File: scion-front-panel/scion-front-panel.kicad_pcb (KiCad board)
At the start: 4 copper layers, 275 x 39.5 mm, 62 parts, among them J1 SEND_VS, J10 SEND_Y3, J11 SEND_U3, J12 SEND_V3, J13 RETURN_Y, J14 RETURN_U, J15 RETURN_V, J16 RETURN_HS, J17 RETURN_VS, J18 Bus_PCI_Express_x4-SCION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

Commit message: getting jiggy with it
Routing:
- net /RETURN_V: track 147.7 -> 175.7 mm
- net /SEND_V1: track 73.5 -> 95.7 mm
- net /SEND_U1: track 78.5 -> 96.0 mm
- net /SEND_V2: track 52.5 -> 66.7 mm
- net /RETURN_U: track 161.9 -> 175.8 mm
- net /SEND_U3: track 36.2 -> 49.0 mm
- net /SEND_V3: track 37.2 -> 49.1 mm
- net /SEND_Y2: track 59.7 -> 66.9 mm
- net /SEND_U2: track 72.1 -> 66.7 mm
- net /SEND_Y3: track 48.7 -> 49.2 mm
- net /RETURN_Y: track 175.4 -> 175.9 mm

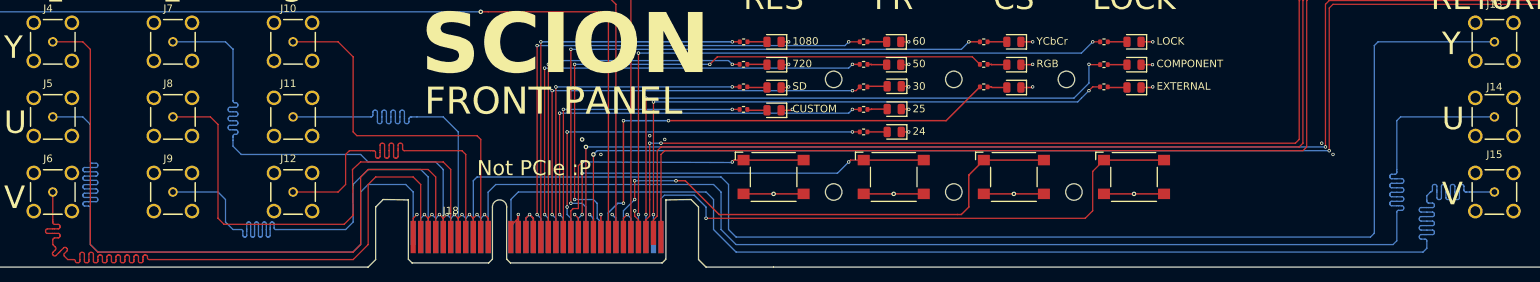
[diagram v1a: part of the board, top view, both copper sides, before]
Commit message: neater squiggles
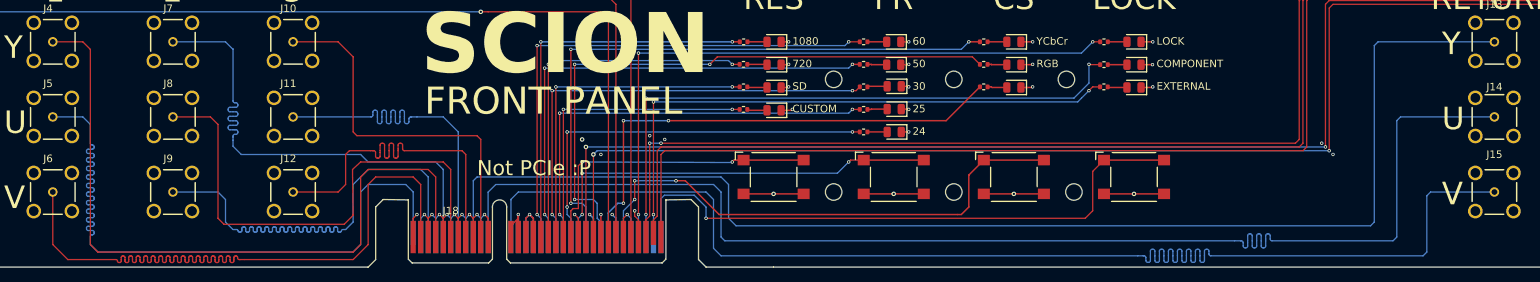
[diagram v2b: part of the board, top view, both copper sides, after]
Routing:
- net /RETURN_U: track 175.8 -> 172.5 mm
- net /RETURN_V: track 175.7 -> 172.6 mm
- net /RETURN_Y: track 175.9 -> 172.9 mm
- net /SEND_U1: track 96.0 -> 95.2 mm

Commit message: fixed LED alignment and gnd filled zone
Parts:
- moved D17 2.30 mm to (288.0, -10.0)
- moved R16 2.23 mm to (292.0, -10.8)
- moved R17 2.23 mm to (292.0, -9.27)
- moved R18 2.23 mm to (292.0, -7.77)
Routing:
- net /SEND_VS: track 138.5 -> 166.7 mm
- net /SEND_HS: track 153.8 -> 167.8 mm
- net /STATUS_B: track 210.1 -> 212.4 mm
- net /STATUS_R: track 202.3 -> 204.6 mm
- net /STATUS_G: track 205.4 -> 207.7 mm
- added copper zone on In1.Cu, net GND
- removed copper zone on In1.Cu, net (none)

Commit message: neat
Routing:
- net /SEND_Y1: track 96.1 -> 94.8 mm
- net /SEND_V1: track 95.5 -> 94.5 mm
- net /SEND_U1: track 95.2 -> 94.3 mm
- net GND: vias 45 -> 46
